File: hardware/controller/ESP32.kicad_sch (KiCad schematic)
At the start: 35 parts, among them J1 Conn_01x05_Pin, Q1 SS8050-G, Q2 SS8050-G, U1 ESP32-S3, Y1 FH4000074Z

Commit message: forgor
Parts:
- added TP17: TCH_CS, SamacSys_Parts:5000, symbol Connector:TestPoint
- added TP18: TCH_IRQ, SamacSys_Parts:5000, symbol Connector:TestPoint
- TP10, TP11, TP12, TP13, TP14, TP15, TP16, TP3, TP5, TP6, TP8, TP9: footprint 5000 -> SamacSys_Parts:5000
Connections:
- net I2C_CTP_LED.~{OE}: now also U1.36 (SPICLK_N/GPIO48); no longer U1.37 (SPICLK_P/GPIO47)
- new net SPI_LCD_SD.TCH_CS: TP17.1
- new net SPI_LCD_SD.TCH_IRQ: TP18.1
- no-connect marks 8 -> 5
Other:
- note added: "ESP32"
- note removed: "todo: look into why some of these power pins do not hvae any decouplihg caps"
- moved on the sheet: AE1, C1, C2, C3, C4, C5, C6, C7, C8, C9, L1, L2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

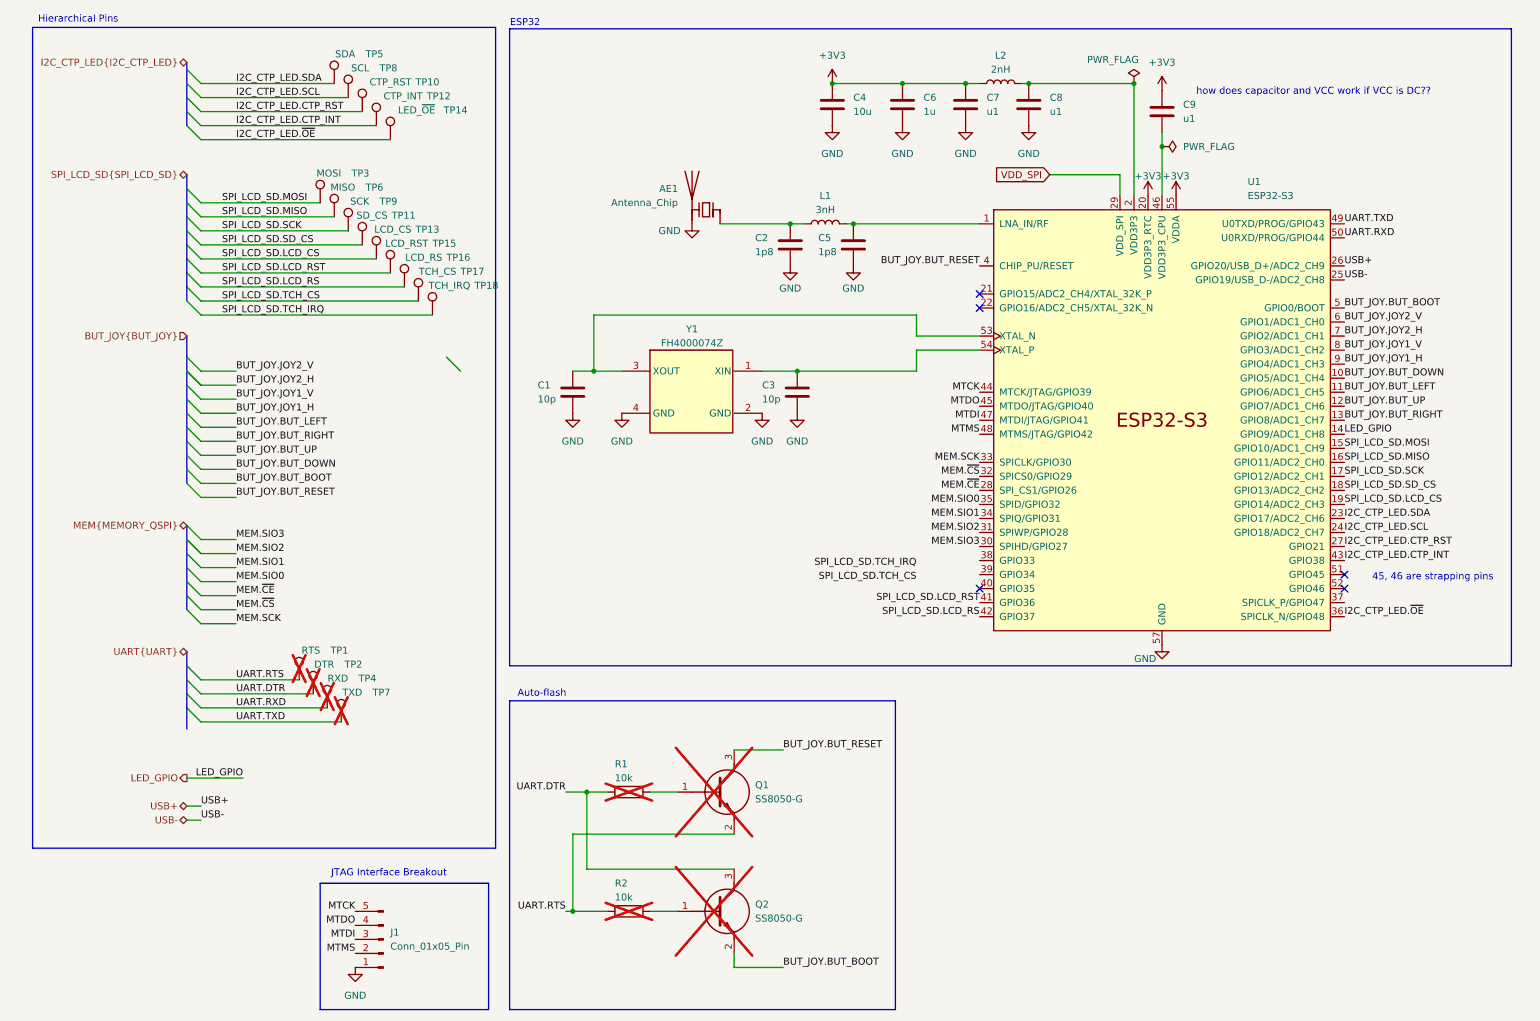
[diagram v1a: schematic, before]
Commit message: clean up DRC. need to add stitching vias and figure out why inner ground plane isnt connected to F.Cu pour
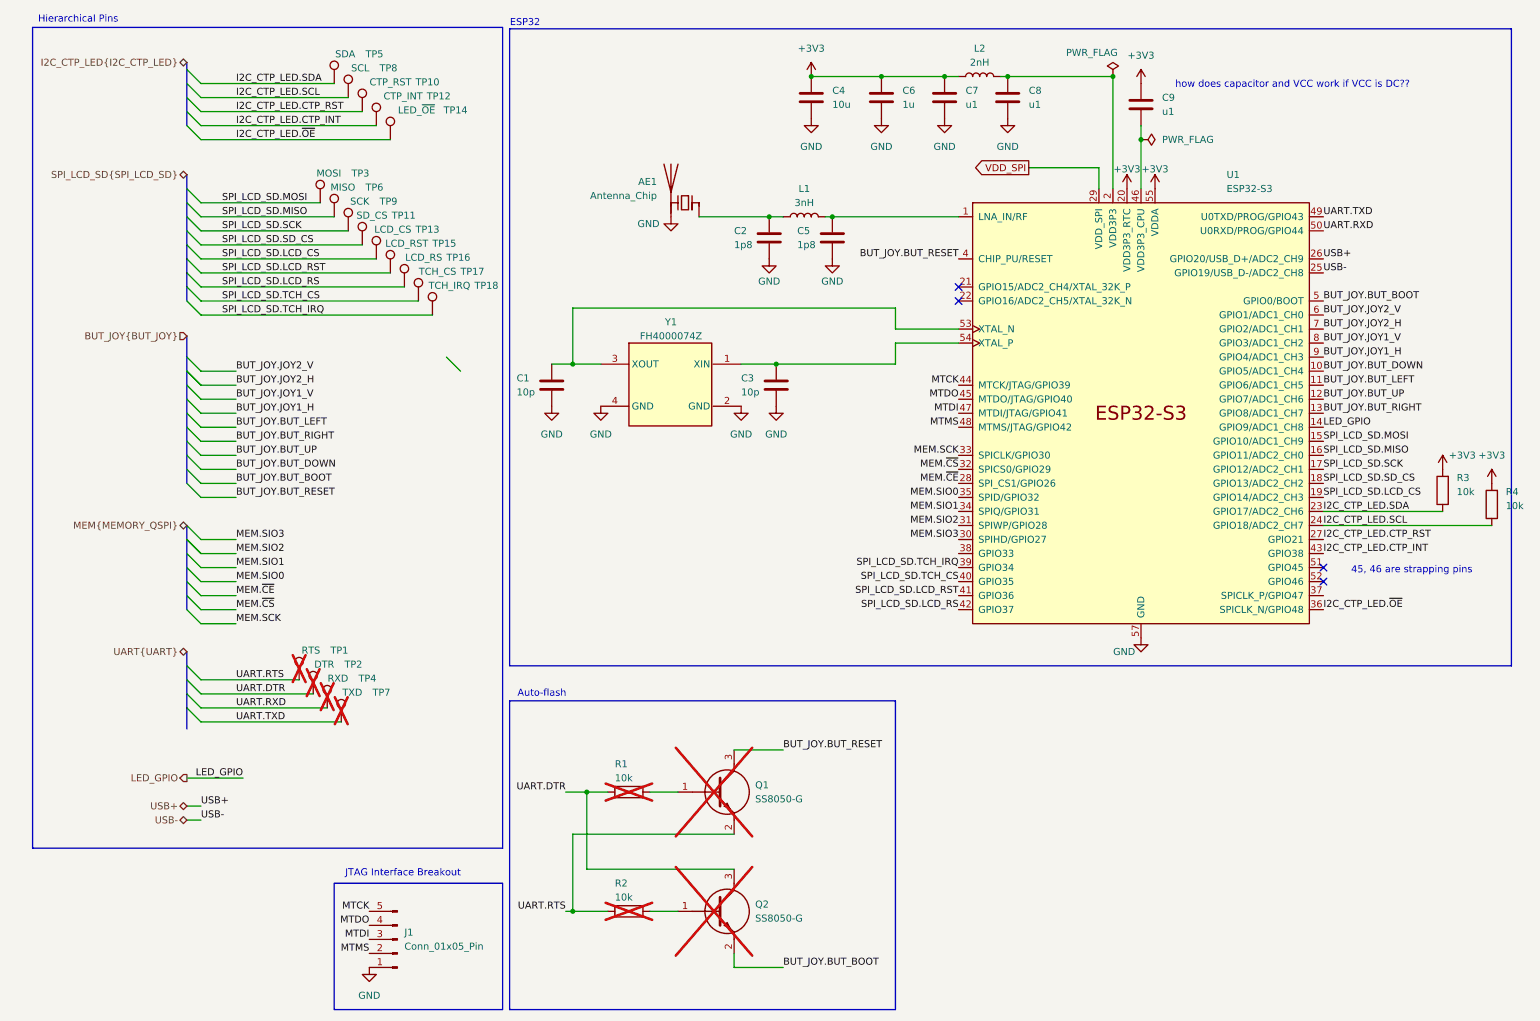
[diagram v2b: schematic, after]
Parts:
- added R3, R4: 10k, SamacSys_Parts:RESC2012X60N, symbol Device:R
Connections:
- net +3V3: now also R3.2, R4.2
- net I2C_CTP_LED.SCL: now also R4.1
- net I2C_CTP_LED.SDA: now also R3.1
- net SPI_LCD_SD.TCH_CS: now also U1.40 (GPIO35)
- net SPI_LCD_SD.TCH_IRQ: now also U1.39 (GPIO34)
- no-connect marks 5 -> 4
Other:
- moved on the sheet: AE1, C1, C2, C3, C4, C5, C6, C7, C8, C9, J1, L1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

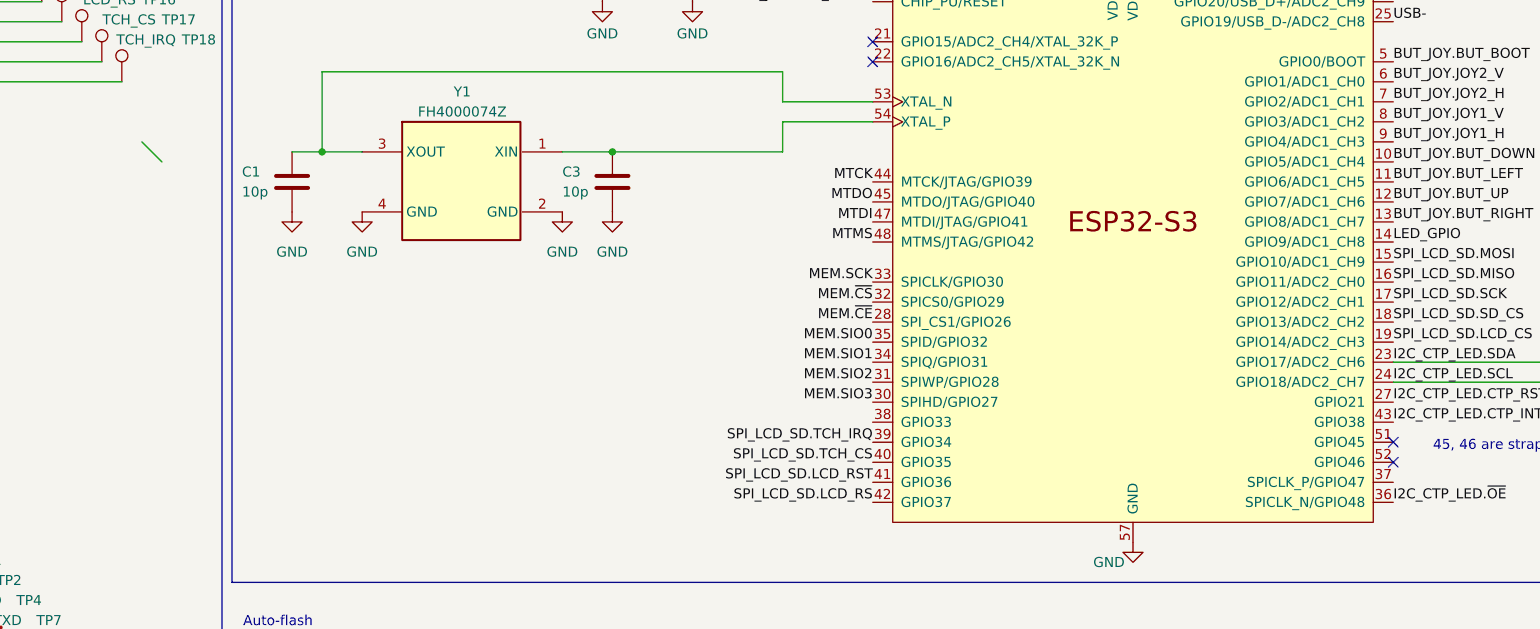
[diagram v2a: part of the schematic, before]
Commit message: save before axing motor driver ic's
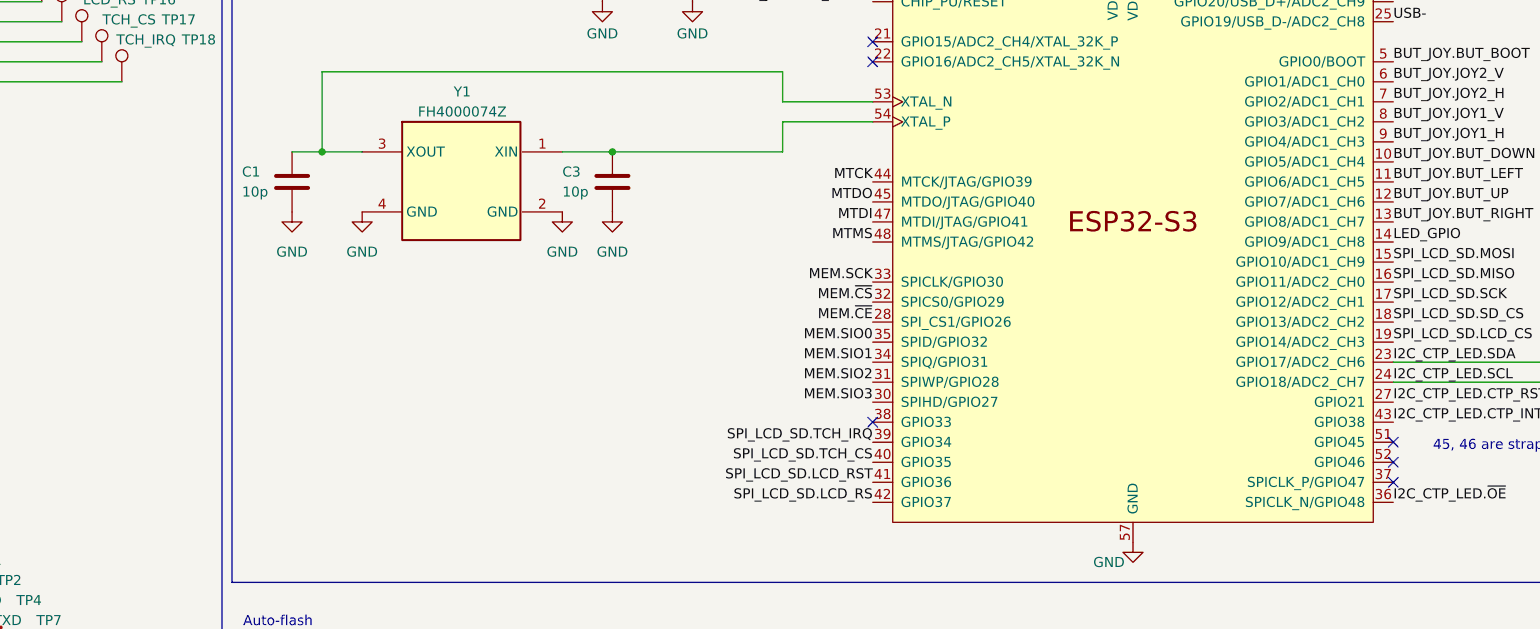
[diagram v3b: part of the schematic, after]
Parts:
- C2, C5: Mouser Price/Stock https://www.mouser.com/ProductDetail/KYOCERA-AVX/KGQ15ACG2A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 -> https://www.mouser.co.uk/ProductDetail/KYOCERA-AVX/KGQ15ACG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
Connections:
- no-connect marks 4 -> 6
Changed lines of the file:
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@@
 	)
 	(no_connect
+		(at 248.92 119.38)
+	)
+	(no_connect
 		(at 182.88 66.04)
 	)
+	(no_connect
+		(at 182.88 111.76)
+	)
 	(bus_entry
 		(at 43.18 111.76)
@@
 	)
 	(bus_entry
-		(at 90.17 76.2)
-		(size 2.54 2.54)
-		(stroke
-			(width 0)
-			(type default)
-		)
-	)
-	(bus_entry
 		(at 43.18 81.28)
 		(size 2.54 2.54)
@@
 			)
 		)
-		(property "Mouser Price/Stock" "https://www.mouser.com/ProductDetail/KYOCERA-AVX/KGQ15ACG2A1R8BT?qs=sGAEpiMZZMsh%252B1woXyUXj17cMikWvs6%2F%252Bbo%2FT8Vs%252Bm0%3D"
+		(property "Mouser Price/Stock" "https://www.mouser.co.uk/ProductDetail/KYOCERA-AVX/KGQ15ACG2A1R8BT?qs=sGAEpiMZZMsh%252B1woXyUXj17cMikWvs6%2F%252Bbo%2FT8Vs%252Bm0%3D"
 			(at 157.48 650.8 0)
 			(effects
@@
 			)
 		)
-		(property "Datasheet" "https://www.mouser.com/datasheet/2/115/DIOD_S_A0002236414_1-2542067.pdf"
+		(property "Datasheet" "https://www.mouser.co.uk/datasheet/2/115/DIOD_S_A0002236414_1-2542067.pdf"
 			(at 162.56 268.58 0)
 			(effects
@@
 			)
 		)
-		(property "Mouser Price/Stock" "https://www.mouser.com/ProductDetail/KYOCERA-AVX/KGQ15ACG2A1R8BT?qs=sGAEpiMZZMsh%252B1woXyUXj17cMikWvs6%2F%252Bbo%2FT8Vs%252Bm0%3D"
+		(property "Mouser Price/Stock" "https://www.mouser.co.uk/ProductDetail/KYOCERA-AVX/KGQ15ACG2A1R8BT?qs=sGAEpiMZZMsh%252B1woXyUXj17cMikWvs6%2F%252Bbo%2FT8Vs%252Bm0%3D"
 			(at 168.91 650.8 0)
 			(effects

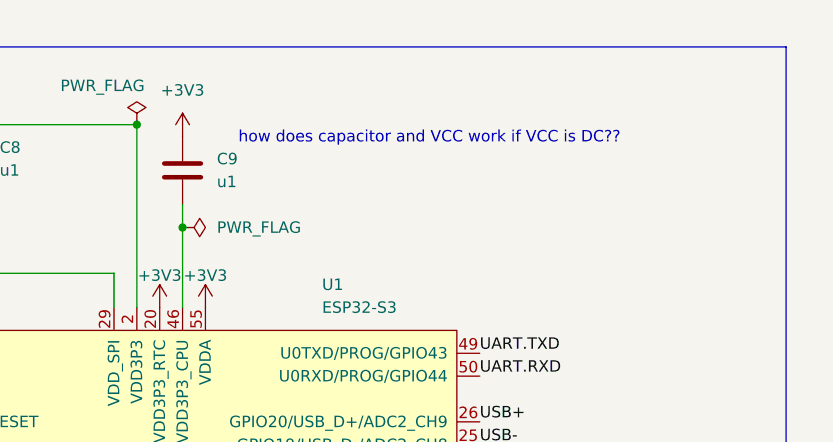
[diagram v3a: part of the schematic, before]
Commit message: axed motor drivers. finished layout for drone but need to review overall system design after reading some stuff
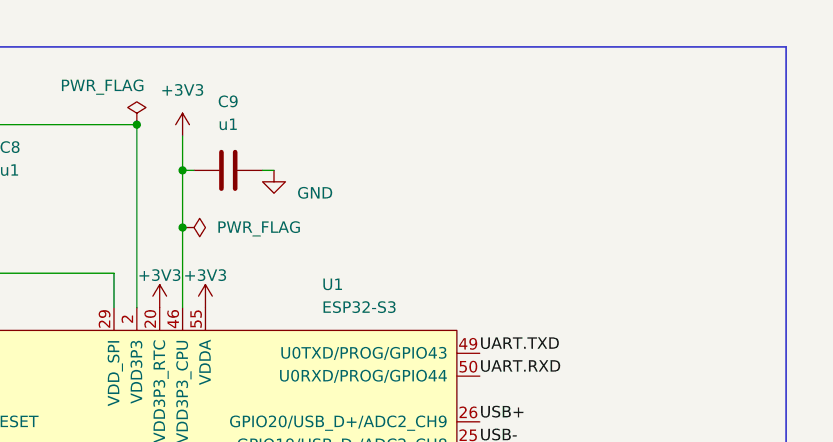
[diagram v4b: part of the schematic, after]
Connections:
- net +3V3: now also U1.46 (VDD3P3_CPU)
- net GND: now also C9.2
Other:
- note removed: "how does capacitor and VCC work if VCC is DC??"
- moved on the sheet: C9
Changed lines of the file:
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@@
 		)
 	)
-	(text "how does capacitor and VCC work if VCC is DC??"
-		(exclude_from_sim no)
-		(at 243.332 26.924 0)
-		(effects
-			(font
-				(size 1.27 1.27)
-			)
-		)
-	)
 	(text "JTAG Interface Breakout"
 		(exclude_from_sim no)
@@
 	)
 	(junction
+		(at 215.9 30.48)
+		(diameter 0)
+		(color 0 0 0 0)
+	)
+	(junction
 		(at 160.02 50.8)
 		(diameter 0)
@@
 		)
 	)
-	(wire
-		(pts
-			(xy 215.9 34.29) (xy 215.9 36.83)
-		)
-		(stroke
-			(width 0)
-			(type default)
-		)
-	)
 	(bus
 		(pts
@@
 	(wire
 		(pts
+			(xy 215.9 26.67) (xy 215.9 30.48)
+		)
+		(stroke
+			(width 0)
+			(type default)
+		)
+	)
+	(wire
+		(pts
 			(xy 45.72 134.62) (xy 63.5 134.62)
 		)
@@
 	(wire
 		(pts
+			(xy 215.9 30.48) (xy 215.9 36.83)
+		)
+		(stroke
+			(width 0)
+			(type default)
+		)
+	)
+	(wire
+		(pts
+			(xy 226.06 30.48) (xy 224.79 30.48)
+		)
+		(stroke
+			(width 0)
+			(type default)
+		)
+	)
+	(wire
+		(pts
 			(xy 45.72 58.42) (xy 77.47 58.42)
 		)
@@
 	(wire
 		(pts
+			(xy 215.9 30.48) (xy 217.17 30.48)
+		)
+		(stroke
+			(width 0)
+			(type default)
+		)
+	)
+	(wire
+		(pts
 			(xy 45.72 142.24) (xy 71.12 142.24)
 		)
@@
 	(symbol
 		(lib_id "Device:C")
-		(at 215.9 30.48 0)
+		(at 220.98 30.48 90)
 		(unit 1)
 		(exclude_from_sim no)
@@
 		(fields_autoplaced yes)
 		(property "Reference" "C9"
-			(at 219.71 29.2099 0)
+			(at 220.98 22.86 90)
 			(effects
 				(font
 					(size 1.27 1.27)
 				)
-				(justify left)
 			)
 		)
 		(property "Value" "u1"
-			(at 219.71 31.7499 0)
+			(at 220.98 25.4 90)
 			(effects
 				(font
 					(size 1.27 1.27)
 				)
-				(justify left)
 			)
 		)
 		(property "Footprint" "SamacSys_Parts:MAJx16"
-			(at 224.79 126.67 0)
+			(at 317.17 21.59 0)
 			(effects
 				(font
@@
 		)
 		(property "Datasheet" "~"
-			(at 224.79 226.67 0)
+			(at 417.17 21.59 0)
 			(effects
 				(font
@@
 		)
 		(property "Description" "Unpolarized capacitor"
-			(at 215.9 30.48 0)
+			(at 220.98 30.48 0)
 			(effects
 				(font
@@
 		)
 		(property "Height" "0.8"
-			(at 224.79 426.67 0)
+			(at 617.17 21.59 0)
 			(effects
 				(font
@@
 		)
 		(property "Mouser Part Number" "963-MAJCH168BB7104KT"
-			(at 224.79 526.67 0)
+			(at 717.17 21.59 0)
 			(effects
 				(font
@@
 		)
 		(property "Mouser Price/Stock" "https://www.mouser.co.uk/ProductDetail/TAIYO-YUDEN/MAJCH168BB7104KTEA01?qs=ZcfC38r4PovaTBrG0IdezQ%3D%3D"
-			(at 224.79 626.67 0)
+			(at 817.17 21.59 0)
 			(effects
 				(font
@@
 		)
 		(property "Manufacturer_Name" "TAIYO YUDEN"
-			(at 224.79 726.67 0)
+			(at 917.17 21.59 0)
 			(effects
 				(font
@@
 		)
 		(property "Manufacturer_Part_Number" "MAJCH168BB7104KTEA01"
-			(at 224.79 826.67 0)
+			(at 1017.17 21.59 0)
 			(effects
 				(font
@@
 					(unit 1)
 				)
+			)
+		)
+	)
+	(symbol
+		(lib_id "power:GND")
+		(at 226.06 30.48 0)
+		(unit 1)
+		(exclude_from_sim no)
+		(in_bom yes)
+		(on_board yes)
+		(dnp no)
+		(property "Reference" "#PWR020"
+			(at 226.06 36.83 0)
+			(effects
+				(font
+					(size 1.27 1.27)
+				)
+				(hide yes)
+			)
+		)
+		(property "Value" "GND"
+			(at 230.632 33.02 0)
+			(effects
+				(font
+					(size 1.27 1.27)
+				)
+			)
+		)
+		(property "Footprint" ""
+			(at 226.06 30.48 0)
+			(effects
+				(font
+					(size 1.27 1.27)
+				)
+				(hide yes)
+			)
+		)
+		(property "Datasheet" ""
+			(at 226.06 30.48 0)
+			(effects
+				(font
+					(size 1.27 1.27)
+				)
+				(hide yes)
+			)
+		)
+		(property "Description" "Power symbol creates a global label with name \"GND\" , ground"
+			(at 226.06 30.48 0)
+			(effects
+				(font
+					(size 1.27 1.27)
+				)
+				(hide yes)
+			)
+		)
+		(pin "1"
+		)
+		(instances
+			(project "controller"
+				(path "/869bea87-c885-4ead-826b-3f34ceacafad/803675b3-25f7-4b49-b465-4697774a1dce"
+					(reference "#PWR020")
+					(unit 1)
+				)
